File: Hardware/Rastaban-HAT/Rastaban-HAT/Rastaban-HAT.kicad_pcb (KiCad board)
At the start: 2 copper layers, 84.3 x 85.4 mm, 92 parts, among them IC1 BCR420UW6-7, IC2 BCM53DS, J1 1778780, J10 GPIO, J11 Conn_01x06_Male, J12 Conn_01x03_Male, J2 1778780, J3 1778780, J4 Screw_Terminal_01x02, J5 Jack-DC 12V+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

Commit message: fixed github
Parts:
- moved JP2 0.50 mm to (103.0, 108.6)
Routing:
- net /FluidMotors/OB2PRI: track 0.00 -> 22.6 mm
- net /FluidMotors/OB1PRI: track 0.00 -> 20.5 mm
- net /FluidMotors/OA1PRI: track 0.00 -> 15.9 mm
- net /FluidMotors/OA2PRI: track 0.00 -> 12.4 mm
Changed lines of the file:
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@@
     (at 132.3465 110.603)
     (property "MANUFACTURER" "Trinamic Motion")
-    (property "Purpose" "Primairy steppermotor driver")
+    (property "Purpose" "Secundary steppermotor driver")
     (property "Sheetfile" "FluidMotors.kicad_sch")
     (property "Sheetname" "FluidMotors")
@@
   )
   (footprint "Jumper:SolderJumper-2_P1.3mm_Open_RoundedPad1.0x1.5mm" (layer "F.Cu")
-    (at 103.4925 108.6)
+    (at 102.997 108.585)
     (descr "SMD Solder Jumper, 1x1.5mm, rounded Pads, 0.3mm gap, open")
     (tags "solder jumper open")
@@
     (at 153.7935 110.407)
     (property "MANUFACTURER" "Trinamic Motion")
-    (property "Purpose" "Primairy steppermotor driver")
+    (property "Purpose" "Focus steppermotor driver")
     (property "Sheetfile" "FocusMotors.kicad_sch")
     (property "Sheetname" "FocusMotors")
@@
     (effects (font (size 1 1) (thickness 0.15)))
   )
+  (segment (start 105.425 123.713) (end 104.902 123.19) (width 0.6) (layer "F.Cu") (net 22))
+  (segment (start 104.902 109.362) (end 107.442 106.822) (width 0.6) (layer "F.Cu") (net 22))
+  (segment (start 109.915 123.713) (end 105.425 123.713) (width 0.6) (layer "F.Cu") (net 22))
+  (segment (start 104.902 123.19) (end 104.902 109.362) (width 0.6) (layer "F.Cu") (net 22))
+  (segment (start 105.702 111.102) (end 107.442 109.362) (width 0.6) (layer "F.Cu") (net 23))
+  (segment (start 112.415 123.013) (end 110.687 121.285) (width 0.6) (layer "F.Cu") (net 23))
+  (segment (start 110.687 121.285) (end 106.172 121.285) (width 0.6) (layer "F.Cu") (net 23))
+  (segment (start 105.702 120.815) (end 105.702 111.102) (width 0.6) (layer "F.Cu") (net 23))
+  (segment (start 112.415 123.713) (end 112.415 123.013) (width 0.6) (layer "F.Cu") (net 23))
+  (segment (start 106.172 121.285) (end 105.702 120.815) (width 0.6) (layer "F.Cu") (net 23))
+  (segment (start 114.915 121.915) (end 107.442 114.442) (width 0.6) (layer "F.Cu") (net 24))
+  (segment (start 114.915 123.713) (end 114.915 121.915) (width 0.6) (layer "F.Cu") (net 24))
+  (segment (start 117.415 121.875) (end 107.442 111.902) (width 0.6) (layer "F.Cu") (net 25))
+  (segment (start 117.415 123.713) (end 117.415 121.875) (width 0.6) (layer "F.Cu") (net 25))
   (zone (net 2) (net_name "GND") (layers F&B.Cu) (hatch edge 0.508)
     (connect_pads (clearance 0.508))

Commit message: started routing V0.2 again
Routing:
- net /FluidMotors/OB2SEC: track 0.00 -> 23.2 mm
- net /FluidMotors/OB1SEC: track 0.00 -> 21.4 mm
- net /FluidMotors/OA1SEC: track 0.00 -> 16.1 mm
- net /FluidMotors/OA2SEC: track 0.00 -> 12.5 mm
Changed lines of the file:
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@@
   (segment (start 117.415 121.875) (end 107.442 111.902) (width 0.6) (layer "F.Cu") (net 25))
   (segment (start 117.415 123.713) (end 117.415 121.875) (width 0.6) (layer "F.Cu") (net 25))
+  (segment (start 128.711 123.717) (end 124.606 123.717) (width 0.6) (layer "F.Cu") (net 26))
+  (segment (start 122.682 110.1075) (end 125.9965 106.793) (width 0.6) (layer "F.Cu") (net 26))
+  (segment (start 124.606 123.717) (end 122.682 121.793) (width 0.6) (layer "F.Cu") (net 26))
+  (segment (start 122.682 121.793) (end 122.682 110.1075) (width 0.6) (layer "F.Cu") (net 26))
+  (segment (start 123.698 111.6315) (end 125.9965 109.333) (width 0.6) (layer "F.Cu") (net 27))
+  (segment (start 131.211 123.717) (end 131.211 123.017) (width 0.6) (layer "F.Cu") (net 27))
+  (segment (start 124.714 121.539) (end 123.698 120.523) (width 0.6) (layer "F.Cu") (net 27))
+  (segment (start 131.211 123.017) (end 129.733 121.539) (width 0.6) (layer "F.Cu") (net 27))
+  (segment (start 129.733 121.539) (end 124.714 121.539) (width 0.6) (layer "F.Cu") (net 27))
+  (segment (start 123.698 120.523) (end 123.698 111.6315) (width 0.6) (layer "F.Cu") (net 27))
+  (segment (start 133.711 123.717) (end 133.711 122.1275) (width 0.6) (layer "F.Cu") (net 28))
+  (segment (start 133.711 122.1275) (end 125.9965 114.413) (width 0.6) (layer "F.Cu") (net 28))
+  (segment (start 136.211 122.0875) (end 125.9965 111.873) (width 0.6) (layer "F.Cu") (net 29))
+  (segment (start 136.211 123.717) (end 136.211 122.0875) (width 0.6) (layer "F.Cu") (net 29))
   (zone (net 2) (net_name "GND") (layers F&B.Cu) (hatch edge 0.508)
     (connect_pads (clearance 0.508))

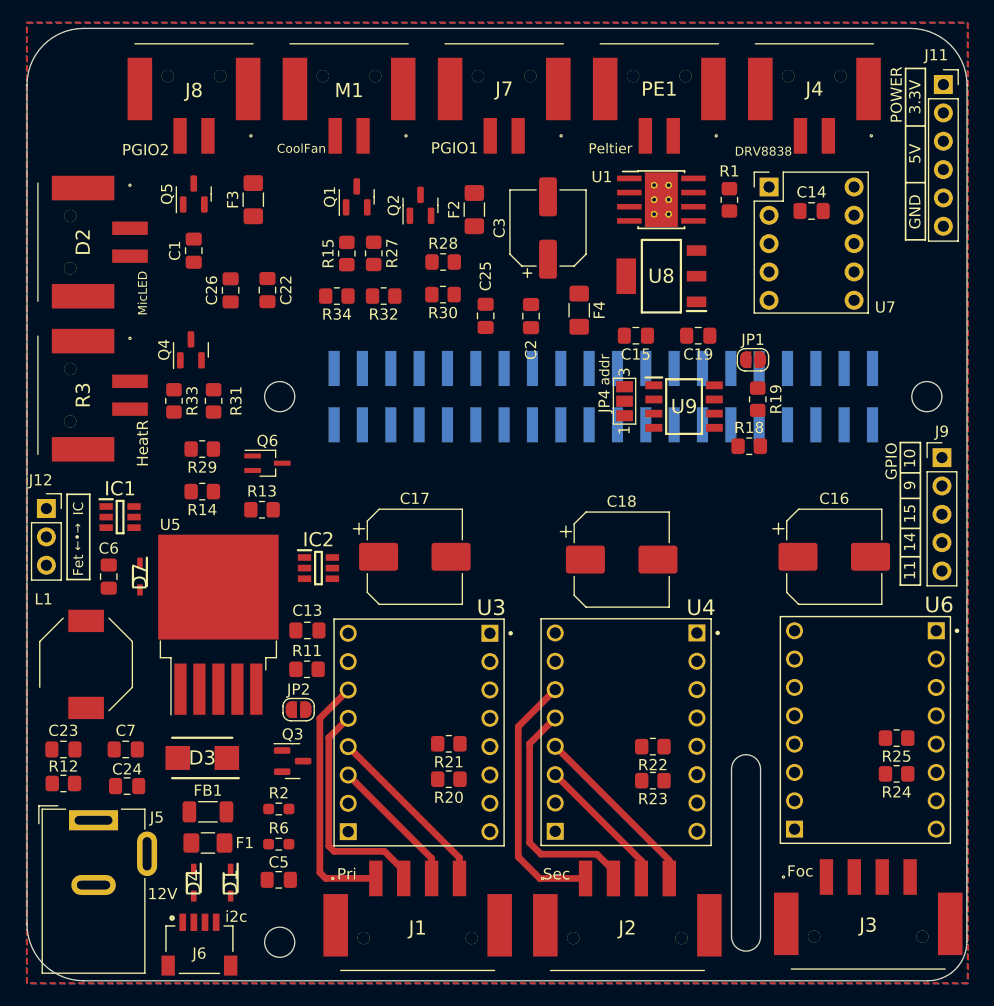
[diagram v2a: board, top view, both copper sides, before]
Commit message: High power lines routed
-i think i got them all at least. width 0.600mm
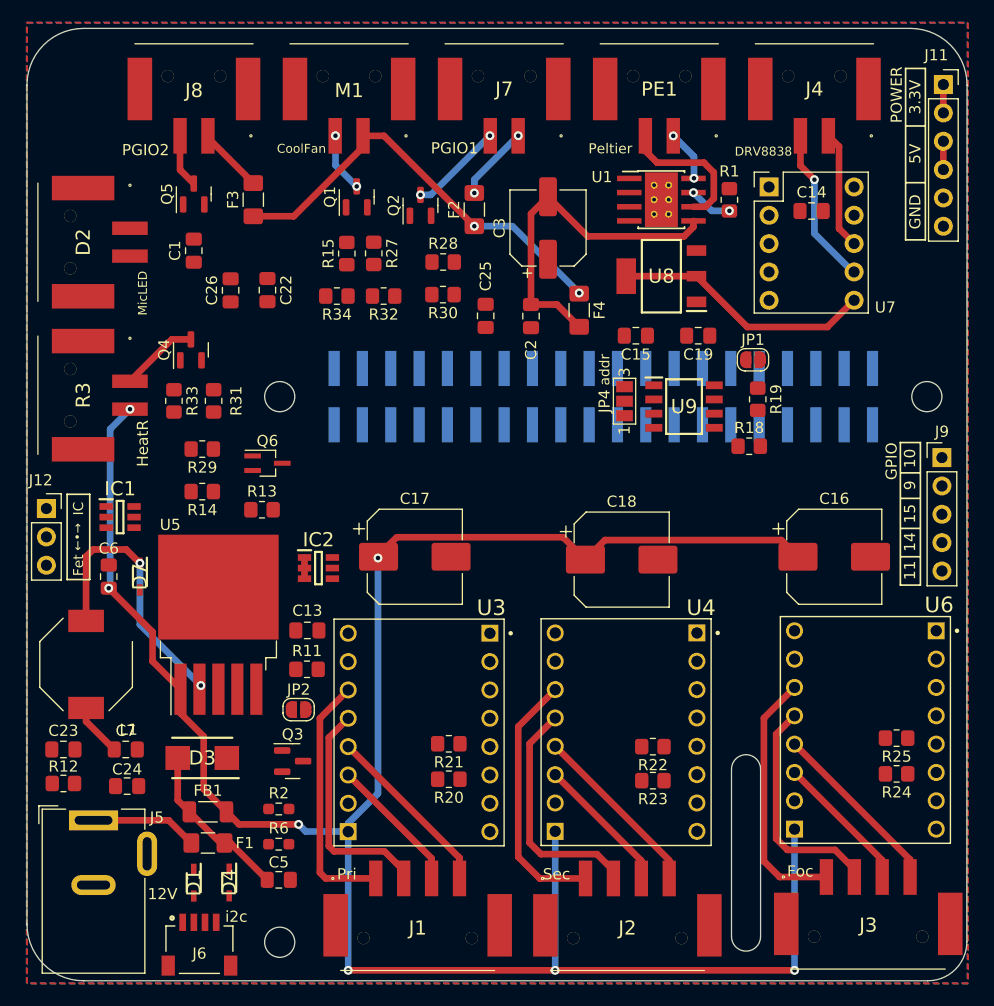
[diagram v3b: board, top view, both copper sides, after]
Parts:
- moved D1 3.30 mm to (93.6, 124.1)
- moved D4 3.18 mm to (96.8, 124.1)
- turned L1 to -90 degrees
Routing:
- net 12V+: track 0.00 -> 235.4 mm, vias 0 -> 9
- net Net-(C2-Pad2): track 0.00 -> 30.8 mm
- net Net-(D7-Pad1): track 0.00 -> 24.6 mm, vias 0 -> 2
- net Net-(C15-Pad2): track 0.00 -> 23.3 mm
- net /FocusMotors/OB2FOCUS: track 0.00 -> 22.9 mm
- net /FocusMotors/OB1FOCUS: track 0.00 -> 20.5 mm
- net /FocusMotors/OA1FOCUS: track 0.00 -> 16.2 mm
- net Net-(C5-Pad1): track 0.00 -> 14.8 mm
- net /FocusMotors/out1: track 0.00 -> 14.3 mm, vias 0 -> 1
- net Net-(PE1-Pad2): track 0.00 -> 12.7 mm
- net /FocusMotors/OA2FOCUS: track 0.00 -> 12.6 mm
- net /FocusMotors/out2: track 0.00 -> 10.6 mm
- net 12VIN: track 0.00 -> 9.61 mm
- net Net-(J7-Pad2): track 0.00 -> 8.45 mm, vias 0 -> 2
- net Net-(Q4-Pad3): track 0.00 -> 7.02 mm
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
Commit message: 5.0V and 3.3V lines finished
-If I did not miss anything
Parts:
- moved Q3 1.12 mm to (101.3, 113.2)
- turned R27 to 90 degrees
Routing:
- net 3.3V+: track 2.54 -> 124.8 mm, vias 0 -> 4
- net 5V+: track 2.54 -> 76.3 mm, vias 0 -> 3
- net Net-(C13-Pad2): track 4.76 -> 46.1 mm, vias 0 -> 5
- net Net-(IC2-Pad4): track 0.00 -> 40.7 mm, vias 0 -> 2
- net Net-(D2-PadK): track 0.00 -> 34.6 mm
- net Net-(J12-Pad1): track 0.00 -> 22.8 mm
- net Net-(IC1-Pad5): track 0.00 -> 13.5 mm
- net Net-(IC2-Pad1): track 1.90 -> 12.4 mm, vias 0 -> 2

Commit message: ERC: errors resolved
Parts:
- removed J12: Conn_01x03_Male, Connector_PinSocket_2.54mm:PinSocket_1x03_P2.54mm_Vertical
- added JP3: Jumper_3_Open, Jumper:SolderJumper-3_P1.3mm_Open_Pad1.0x1.5mm_NumberLabels, F.Cu at (113.0, 77.8)
- added JP5: Jumper_3_Open, Jumper:SolderJumper-3_P1.3mm_Open_Pad1.0x1.5mm_NumberLabels, F.Cu at (80.6, 92.2)
- added U2: TLV1117-33, SamacSys_Parts:SOT230P700X180-4N, F.Cu at (113.2, 83.6)
- moved C1 27.1 mm to (118.0, 79.2), turned to -90 degrees
- moved R22 3.16 mm to (134.7, 115.1)
- moved R23 3.06 mm to (134.7, 111.9)
- moved C23 0.14 mm to (81.9, 112.0), turned to 180 degrees
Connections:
- C1 pad 1: 3.3V+ -> Net-(C1-Pad1)
- D2 pad A: 3.3V+ -> Net-(D2-PadA)
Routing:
- net 3.3V+: track 124.8 -> 313.5 mm, vias 4 -> 14
- net ENPRI: track 0.00 -> 79.1 mm
- net SCL: track 0.00 -> 65.9 mm, vias 0 -> 1
- net ENSEC: track 0.00 -> 64.1 mm, vias 0 -> 1
- net GPIO14: track 0.00 -> 59.0 mm, vias 0 -> 2
- net CTRLLED: track 0.00 -> 54.4 mm, vias 0 -> 3
- net GPIO15: track 0.00 -> 54.1 mm, vias 0 -> 1
- net CTRLHEAT: track 0.00 -> 54.0 mm, vias 0 -> 3
- net CTRLFAN: track 0.00 -> 53.2 mm, vias 0 -> 3
- net SDA: track 0.00 -> 52.6 mm, vias 0 -> 1
- net 5V+: track 76.3 -> 127.9 mm, vias 3 -> 4
- net ENFOC: track 0.00 -> 50.5 mm, vias 0 -> 2
- net Net-(IC1-Pad6): track 0.00 -> 48.8 mm, vias 0 -> 4
- net SLEEP: track 0.00 -> 43.9 mm, vias 0 -> 1
- net GND: track 0.00 -> 41.7 mm, vias 0 -> 44
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
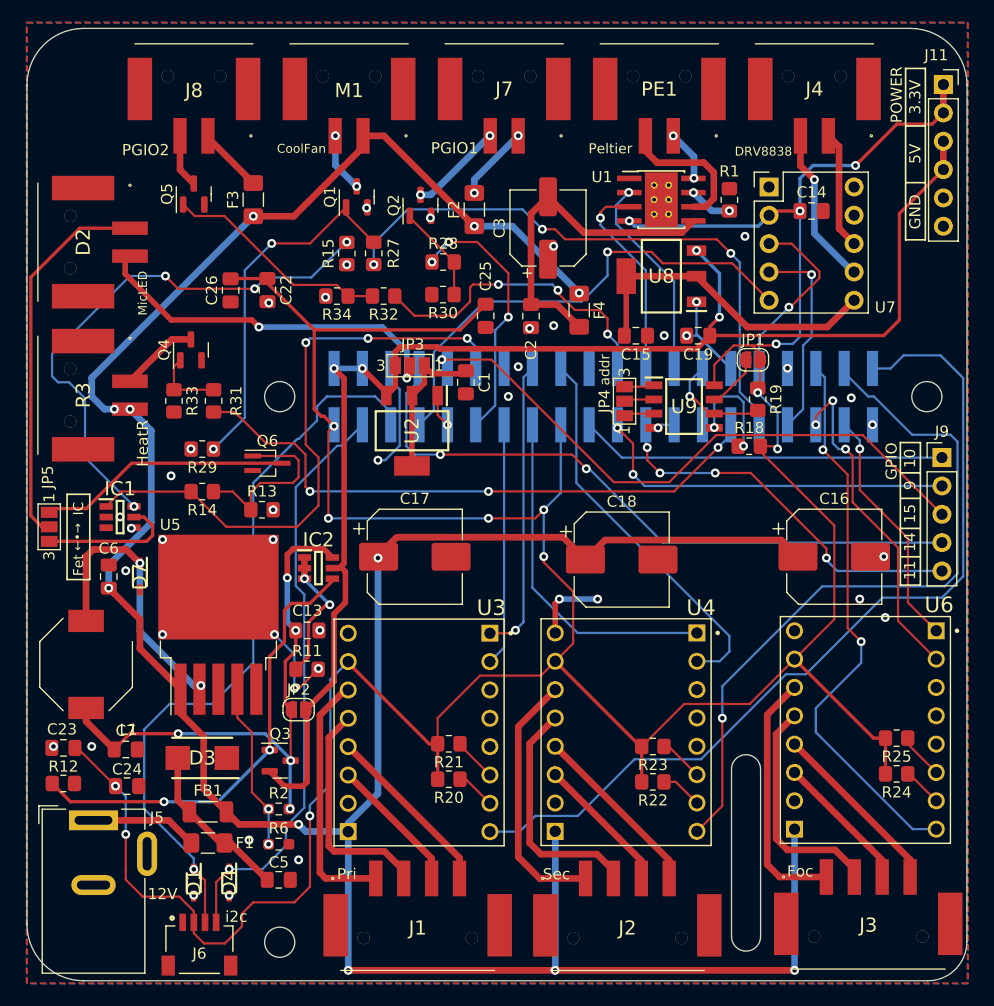
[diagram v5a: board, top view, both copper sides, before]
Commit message: ERC cleared
- 0 errors
- 0 warnings
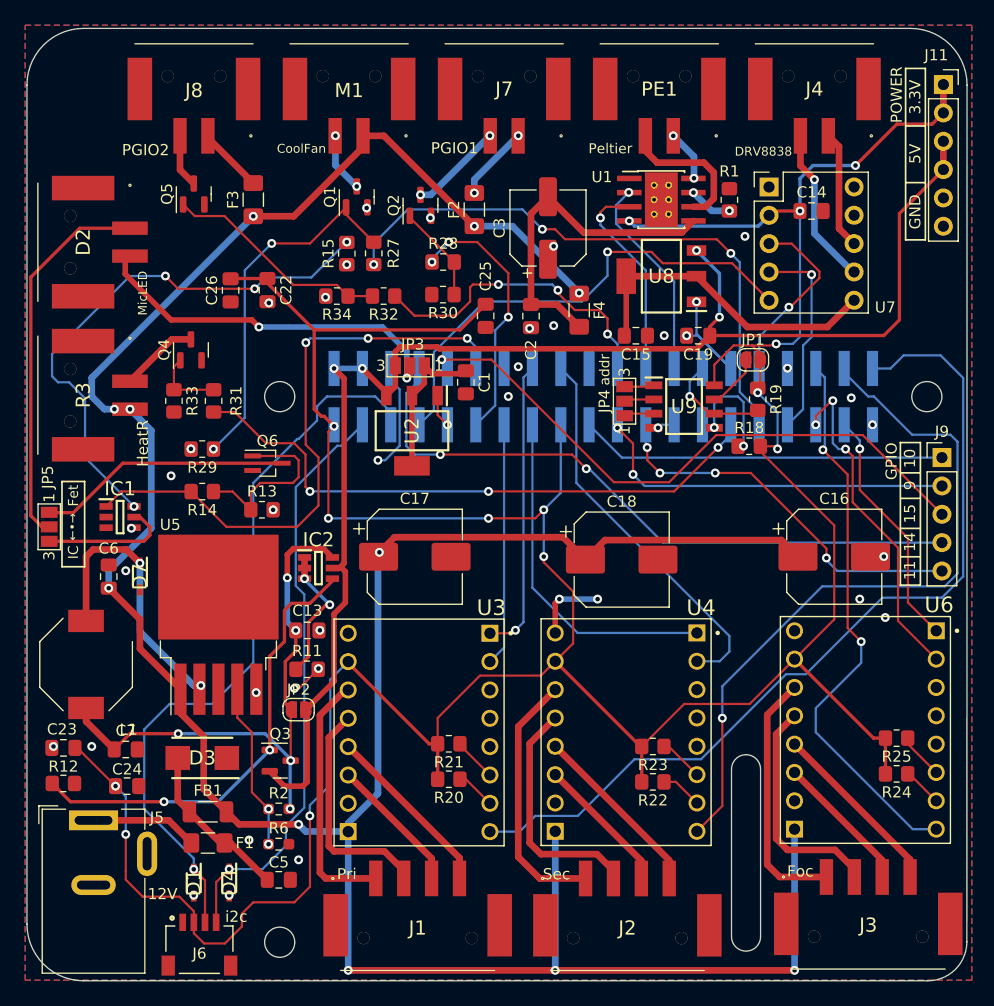
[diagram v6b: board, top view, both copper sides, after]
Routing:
- net GND: track 41.7 -> 36.1 mm, vias 44 -> 40
- net Net-(IC1-Pad5): track 12.3 -> 11.8 mm
- removed copper zone on B.Cu, net (none)
- removed copper zone on F.Cu, net (none)

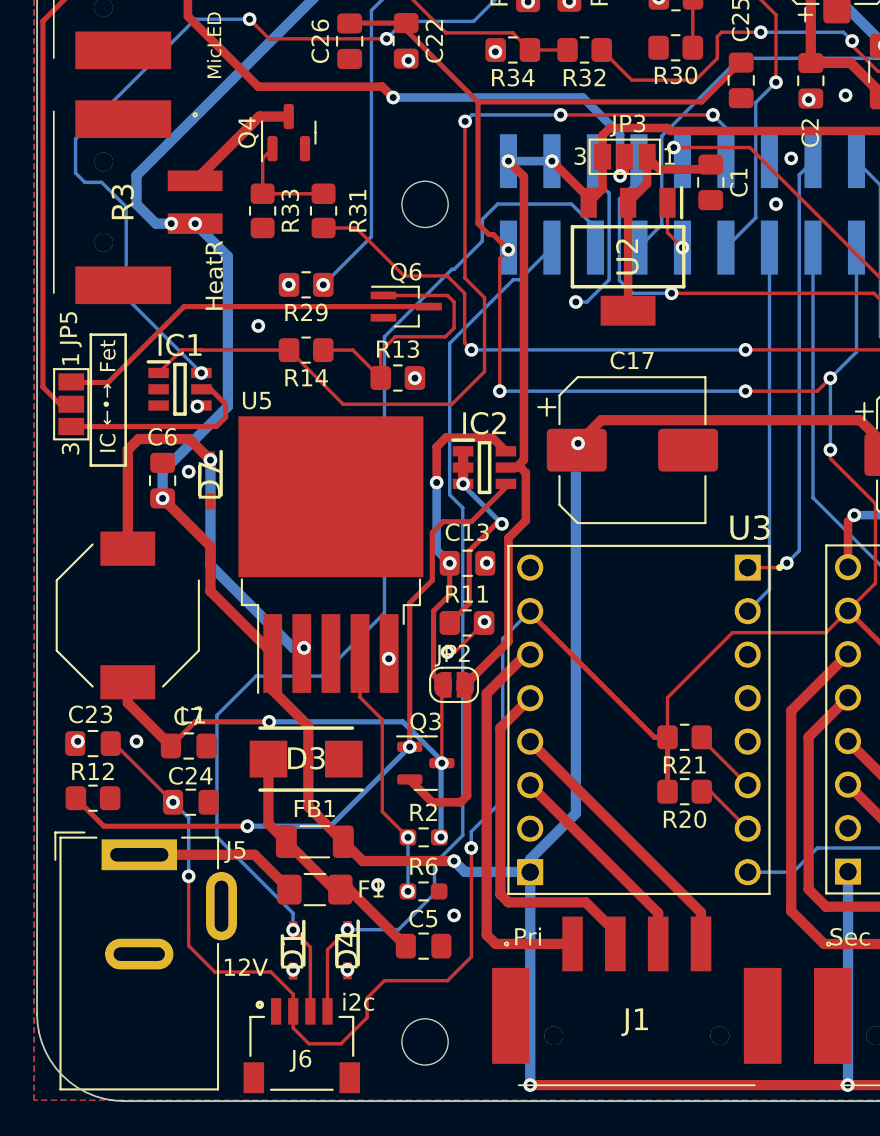
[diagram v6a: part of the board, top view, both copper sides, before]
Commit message: improved silkscreen
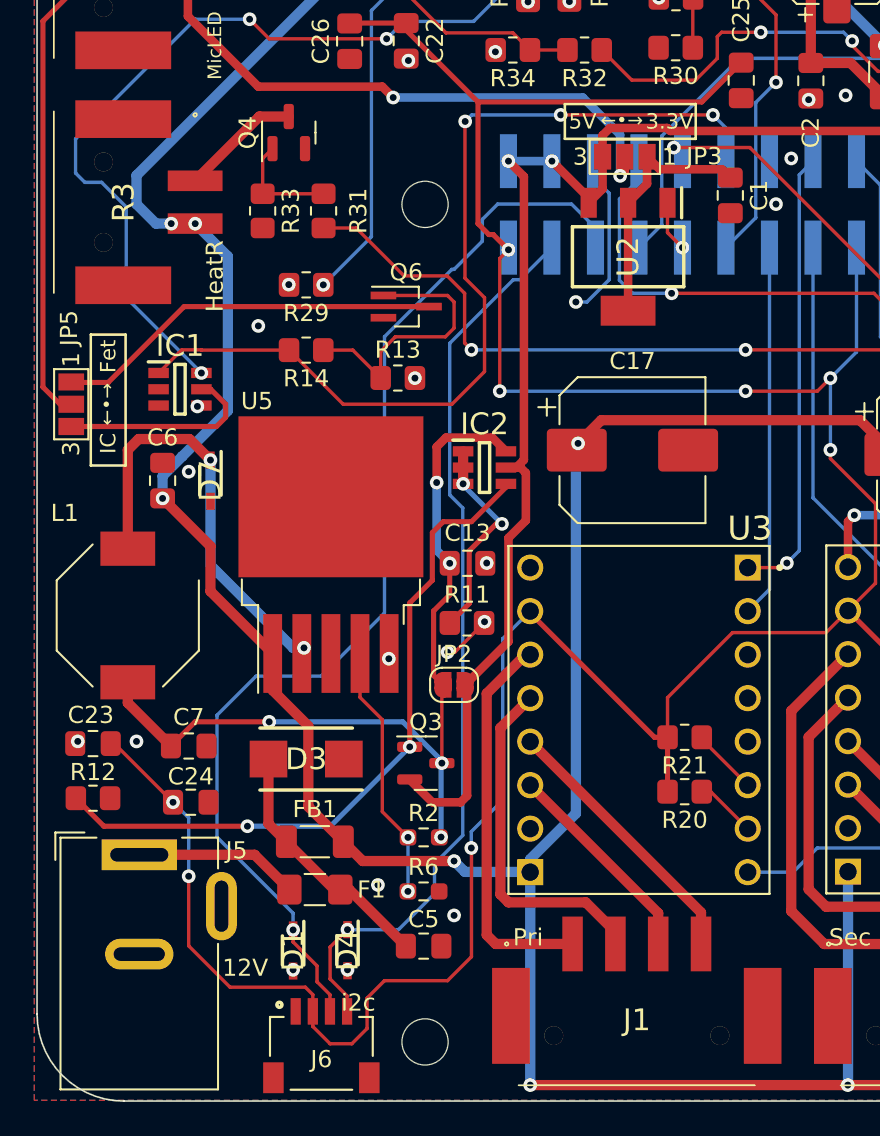
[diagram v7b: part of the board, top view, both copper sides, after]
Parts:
- moved C1 1.37 mm to (119.1, 80.0)
- moved J6 1.14 mm to (95.2, 127.7)
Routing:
- net Net-(C1-Pad1): track 13.6 -> 14.8 mm
